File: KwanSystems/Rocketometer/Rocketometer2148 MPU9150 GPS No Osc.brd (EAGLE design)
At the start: 55.9 x 22.9 mm, 62 parts, among them J001 USB_MICROB_JSTGCT, J301 JST 2mm, J401 M07, J501 GP-2106, J701 MICROSD-SOCKET, Q050 PMOS, U101 BMP180, U201 5319 3.3V, U301 73831, U401 LPC2148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

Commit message: Finally found a complete solution
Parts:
- removed U$5: (no value), KwanSystems:KWAN_ACC
- removed U$6: (no value), KwanSystems:OSHW_ACC
- moved C101 14.5 mm to (22.4, 16.8), turned to 270 degrees
- moved U101 10.8 mm to (19.3, 16.8), turned to 270 degrees
- moved C901 9.37 mm to (3.81, 11.4), flipped to the bottom, turned to 270 degrees
- moved U902 7.98 mm to (7.62, 11.4), flipped to the bottom
- moved C906 7.18 mm to (11.2, 11.4), flipped to the bottom, turned to 270 degrees
- moved D301 1.80 mm to (45.2, 10.2), turned to 90 degrees
- moved D050 1.05 mm to (45.2, 8.64), turned to 90 degrees
- moved R015 1.02 mm to (47.2, 7.37)
- moved C023 0.51 mm to (50.0, 9.40), flipped to the top
- moved R023 0.51 mm to (50.0, 11.2), flipped to the top
- moved R053 0.51 mm to (47.8, 9.40), flipped to the top
- flipped C301 to the top
- flipped J001 to the top, turned to 90 degrees
- flipped J301 to the bottom, turned to 90 degrees
- turned Q050 to 180 degrees
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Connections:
- removed net N$6: D050.A, Q050.3, R053.1
- removed net N$7: D050.C, R053.3
- new net USBLIGHT+: D050.A, R053.7
- new net USBON+: Q050.3, R053.2, R053.8
- net CHARGE_STAT+: now also R053.6; no longer R053.2
- net CONN_D+: now also R023.4, R053.1; no longer R023.2, R053.8
- net CONN_D-: now also R023.3; no longer R023.1
- net GND: now also D050.C; no longer R053.6
- net USBD+: now also R023.1; no longer R023.3
- net USBD-: now also R023.2; no longer R023.4
- net USB_SOFTCONNECT: now also R015.1; no longer R015.4
- net VBUS: now also R053.3; no longer R053.7
- net VCC: now also R015.4; no longer R015.1
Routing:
- net VCC: track 0.00 -> 143.4 mm, vias 0 -> 9
- net EXT: track 0.00 -> 66.8 mm, vias 0 -> 3
- net SDA0: track 0.00 -> 51.7 mm, vias 0 -> 4
- net SCL0: track 0.00 -> 49.0 mm, vias 0 -> 3
- net 1.8V: track 0.00 -> 40.2 mm, vias 0 -> 4
- net VBUS: track 0.00 -> 40.0 mm, vias 0 -> 3
- net USB_SOFTCONNECT: track 0.00 -> 36.6 mm, vias 0 -> 1
- net VLIPO: track 0.00 -> 36.6 mm, vias 0 -> 3
- net PPS: track 0.00 -> 32.2 mm, vias 0 -> 2
- net EN: track 0.00 -> 31.1 mm, vias 0 -> 3
- net ONOFF: track 0.00 -> 30.5 mm, vias 0 -> 2
- net RX_GPS: track 0.00 -> 28.2 mm, vias 0 -> 2
- net TX_GPS: track 0.00 -> 26.8 mm, vias 0 -> 3
- net ACCINT: track 0.00 -> 26.5 mm, vias 0 -> 2
- net RESET: track 0.00 -> 24.2 mm, vias 0 -> 4
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
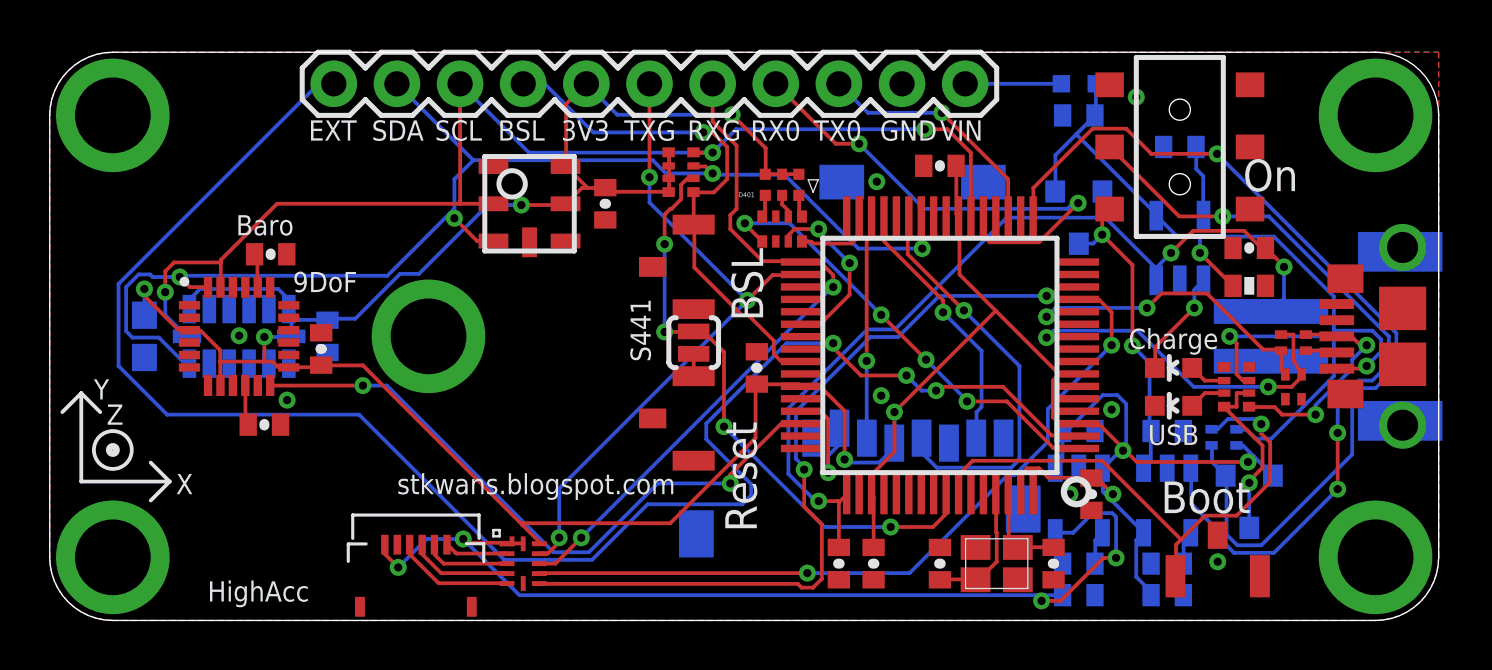
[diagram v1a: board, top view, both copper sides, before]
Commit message: Added new feature to NavCalc
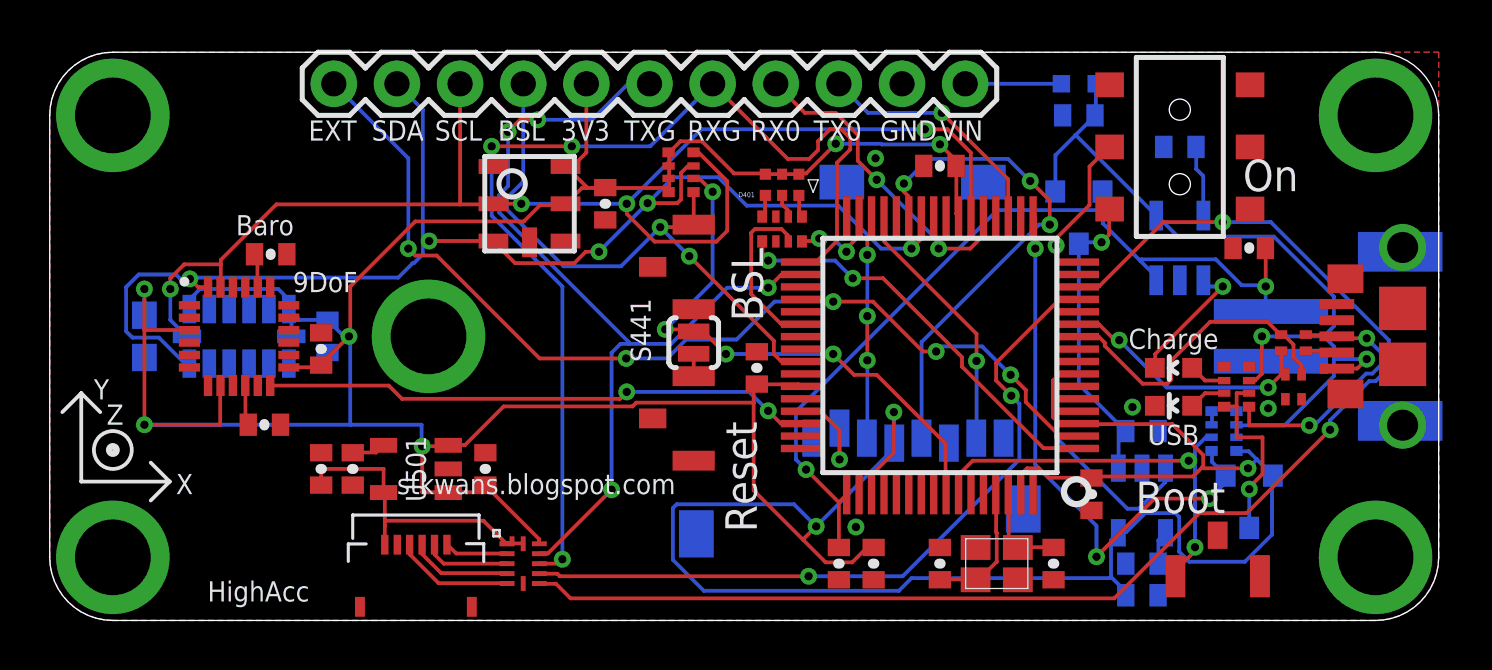
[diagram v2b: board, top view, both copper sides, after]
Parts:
- removed R011: 100k, SparkFun:0402-RES
- R015: device KwanSystems:CRA02 -> KwanSystems:CRA04
- moved C505 30.9 mm to (10.9, 6.10), flipped to the top, turned to 90 degrees
- moved C504 29.5 mm to (12.2, 6.10), flipped to the top, turned to 270 degrees
- moved U501 26.7 mm to (14.7, 6.10), flipped to the top, turned to 90 degrees
- moved C501 23.9 mm to (17.5, 6.10), flipped to the top, turned to 90 degrees
- moved C201 1.02 mm to (43.9, 7.62)
- moved C204 1.02 mm to (43.9, 2.29)
- moved C205 1.02 mm to (43.9, 1.02)
- moved U201 1.02 mm to (43.9, 4.83)
- moved R015 0.25 mm to (47.2, 7.62)
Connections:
- removed net BATLVL: U401.15
- new net N$3: R015.3, R015.4
- net GND: now also R015.5; no longer R011.1
- net VBUS: now also R015.6, R015.7; no longer R011.2, R015.3
- net VCC: now also R015.8; no longer R015.4
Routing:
- net VCC: track 143.4 -> 187.9 mm
- net 1.8V: track 40.2 -> 12.3 mm, vias 4 -> 0
- net EXT: track 66.8 -> 40.3 mm, vias 3 -> 5
- net PPS: track 32.2 -> 55.1 mm
- net RX_GPS: track 28.2 -> 42.5 mm, vias 2 -> 3
- net USB_SOFTCONNECT: track 36.6 -> 22.7 mm, vias 1 -> 3
- net EN: track 31.1 -> 19.2 mm, vias 3 -> 1
- net TX_GPS: track 26.8 -> 35.7 mm, vias 3 -> 4
- net RX0: track 19.7 -> 12.9 mm
- net SCL0: track 49.0 -> 55.1 mm, vias 3 -> 4
- net VBUS: track 40.0 -> 34.2 mm, vias 3 -> 2
- net USB_ON: track 22.1 -> 16.9 mm, vias 1 -> 2
- net ACCINT: track 26.5 -> 22.2 mm
- net SCK0: track 16.6 -> 20.3 mm, vias 1 -> 3
- net BSL: track 21.3 -> 24.0 mm, vias 1 -> 2
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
